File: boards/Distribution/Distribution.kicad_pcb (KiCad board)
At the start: 2 copper layers, 30 x 35 mm, 12 parts, among them CN1 B2PS-VH, CN2 Grove, CN3 B3B-ZR, CN4 B3B-ZR, CN5 B3B-ZR, CN6 B3B-ZR, U1 OKL-T/6-W12N

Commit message: modify PCB design
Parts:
- CN2: footprint Connector_JST:JST_PH_B4B-PH-K_1x04_P2.00mm_Vertical -> Grove:GROVE-HW4-2.0
- moved CN2 3.00 mm to (68.5, 53.2), turned to 0 degrees
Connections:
- CN2 pad 1: GND -> /SERIAL1
- CN2 pad 2: 5VM -> /SERIAL2
- CN2 pad 3: /SERIAL2 -> 5VM
- CN2 pad 4: /SERIAL1 -> GND
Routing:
- net 5VM: track 28.8 -> 27.4 mm

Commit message: modify PCB design
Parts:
- U1: value OKL-T/6-W12N -> OKL-T/3-W12N
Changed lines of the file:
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@@
 			)
 		)
-		(property "Value" "OKL-T/6-W12N"
+		(property "Value" "OKL-T/3-W12N"
 			(at -2.54 2.54 0)
 			(unlocked yes)

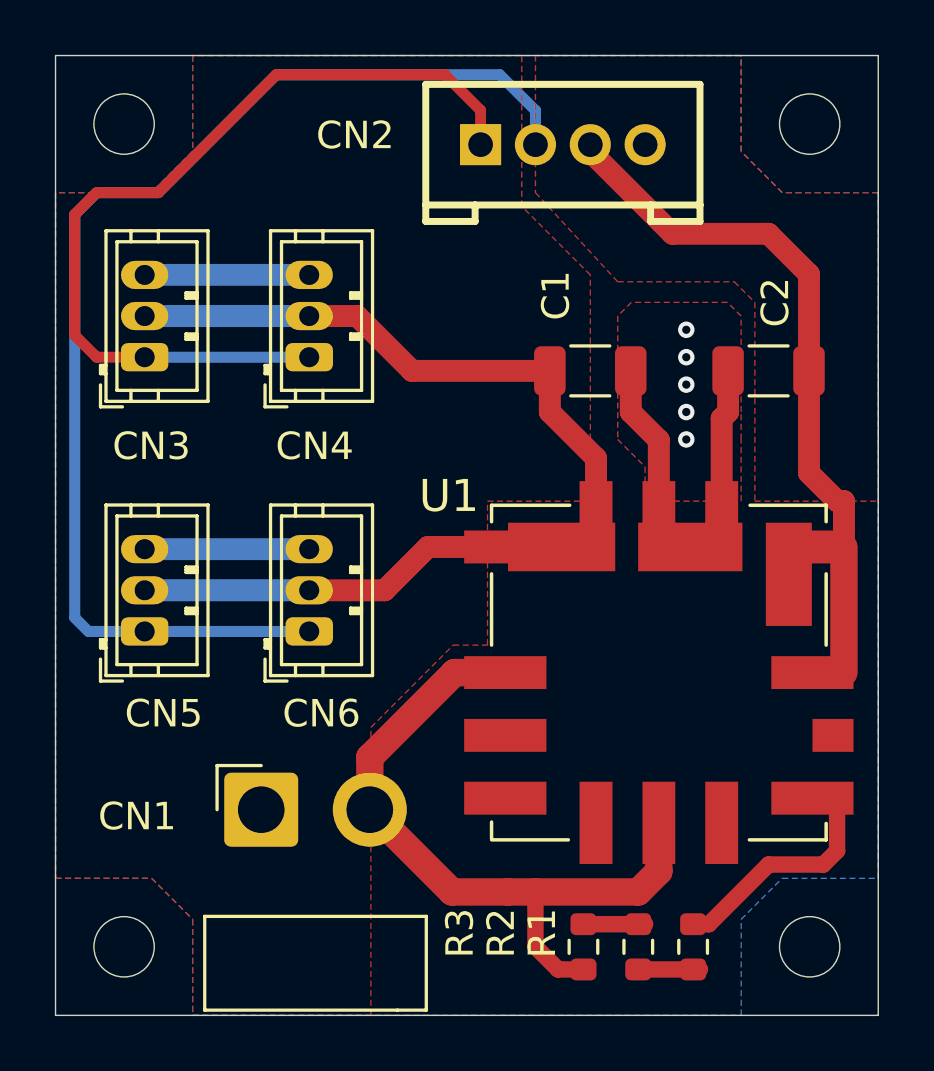
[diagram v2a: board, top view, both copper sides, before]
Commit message: modify PCB design for DRC
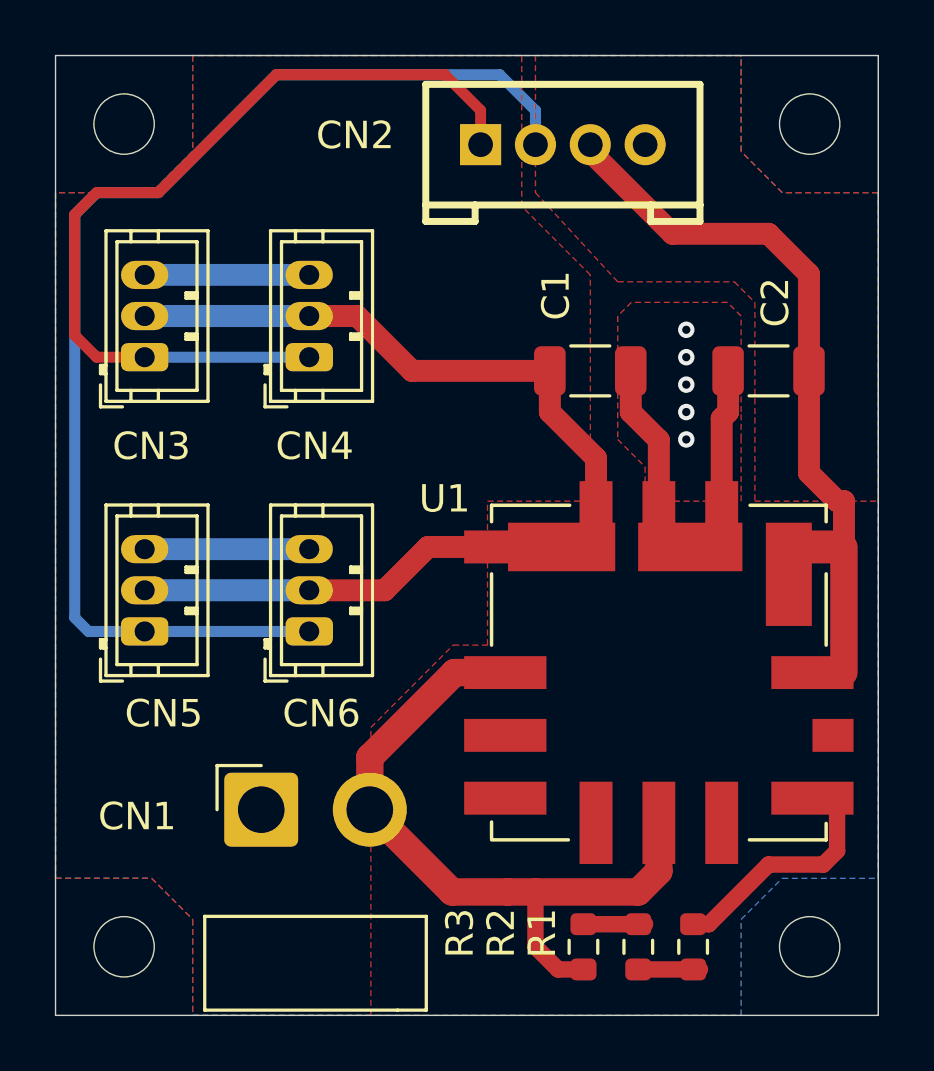
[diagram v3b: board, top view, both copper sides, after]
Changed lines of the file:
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@@
 			(effects
 				(font
-					(size 1.1684 1.1684)
-					(thickness 0.1016)
+					(size 1 1)
+					(thickness 0.15)
 				)
 				(justify left bottom)
